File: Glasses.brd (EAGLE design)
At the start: 139.7 x 63.5 mm, 0 parts

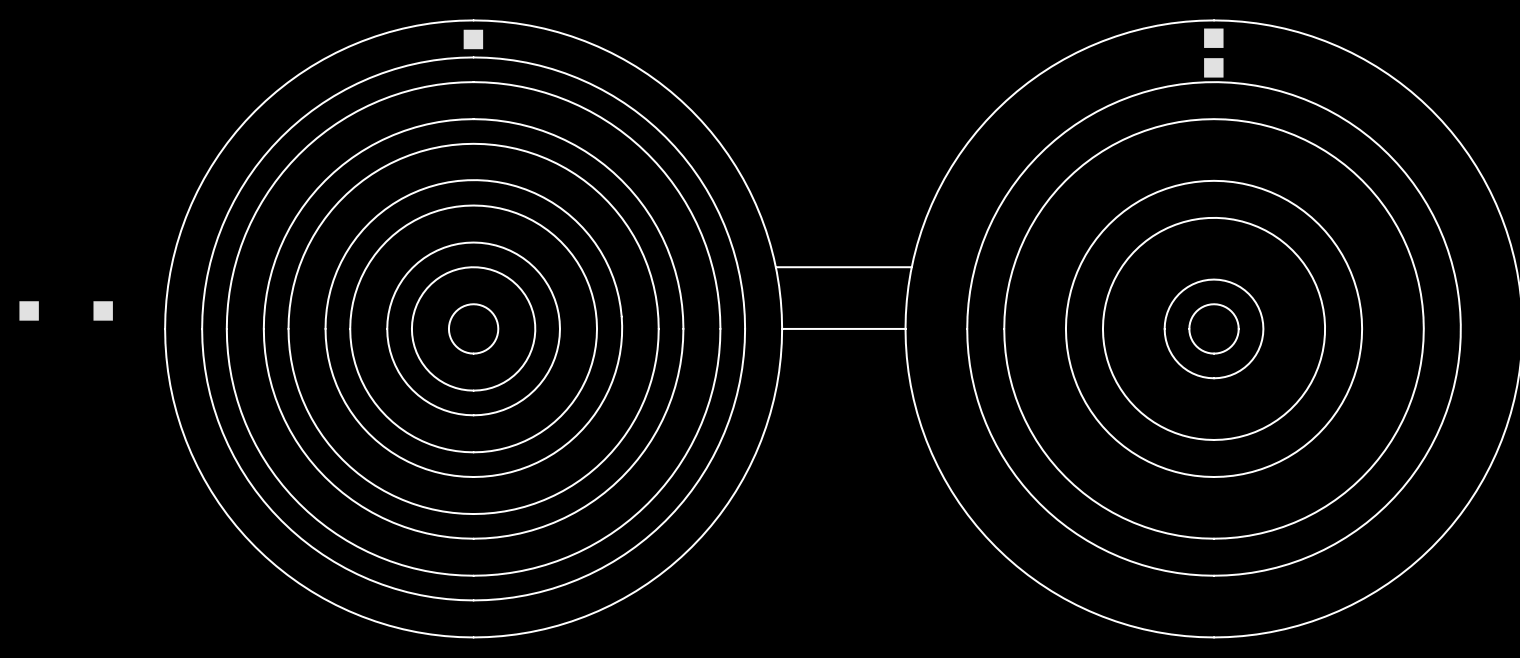
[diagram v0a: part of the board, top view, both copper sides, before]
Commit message: began laying out glasses shape
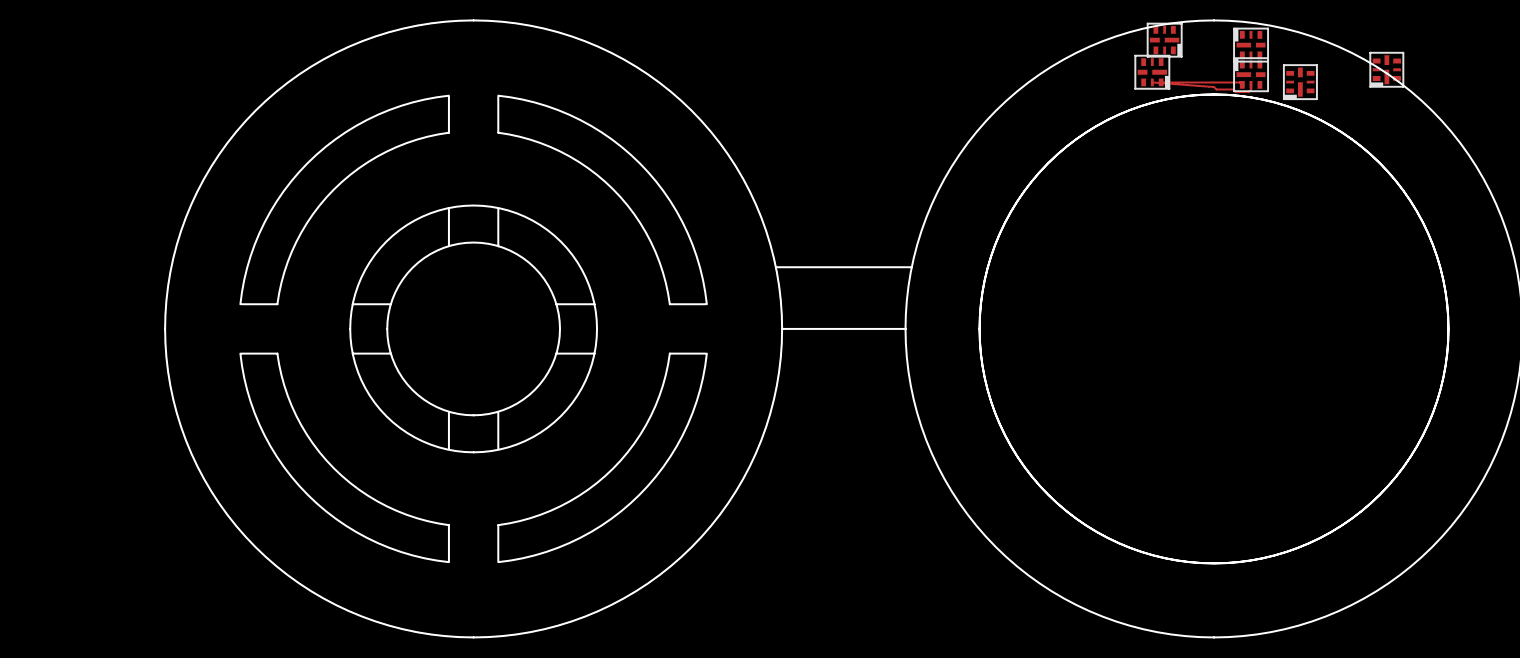
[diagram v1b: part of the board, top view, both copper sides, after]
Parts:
- added FRAME1: FRAME-LETTERNO_PACKAGE, SparkFun-Aesthetics:DUMMY
- added U1, U2, U3, U4, U5, U6: APA1022020, 1_BES_Optoelectronics:APA102-2020
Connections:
- new net GND: U1.GND, U1.GNDPAD, U2.GND, U2.GNDPAD, U3.GND, U3.GNDPAD, U4.GND, U4.GNDPAD, U5.GND, U5.GNDPAD, U6.GND, U6.GNDPAD
- new net N$1: U1.SDO, U2.SDI
- new net N$10: U5.SDO, U6.SDI
- new net N$2: U1.CKO, U2.CKI
- new net N$3: U2.CKO, U3.CKI
- new net N$4: U2.SDO, U3.SDI
- new net N$5: U3.SDO, U4.SDI
- new net N$6: U3.CKO, U4.CKI
- new net N$7: U4.CKO, U5.CKI
- new net N$8: U4.SDO, U5.SDI
- new net N$9: U5.CKO, U6.CKI
- new net VCC: U1.VDD, U1.VDDPAD, U2.VDD, U2.VDDPAD, U3.VDD, U3.VDDPAD, U4.VDD, U4.VDDPAD, U5.VDD, U5.VDDPAD, U6.VDD, U6.VDDPAD
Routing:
- net N$3: track 0.00 -> 11.0 mm
- net N$4: track 0.00 -> 8.47 mm
- added copper zone on layer 1, net N$11
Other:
- outline, holes or cut-outs redrawn

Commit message: Post-print changes
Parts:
- moved U1 32.4 mm to (105.4, 29.2), turned to 45 degrees
- moved U5 27.9 mm to (128.3, 82.5)
- moved U3 27.4 mm to (118.1, 84.6)
- moved U4 26.7 mm to (110.5, 34.3), turned to 45 degrees
- moved U6 25.3 mm to (133.3, 82.5)
- moved U2 24.2 mm to (105.4, 34.3), turned to 135 degrees
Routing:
- net N$3: track 11.0 -> 0.00 mm
- net N$4: track 8.47 -> 0.00 mm
- added copper zone on layer 1, net GND
- removed copper zone on layer 1, net N$11
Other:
- outline, holes or cut-outs redrawn

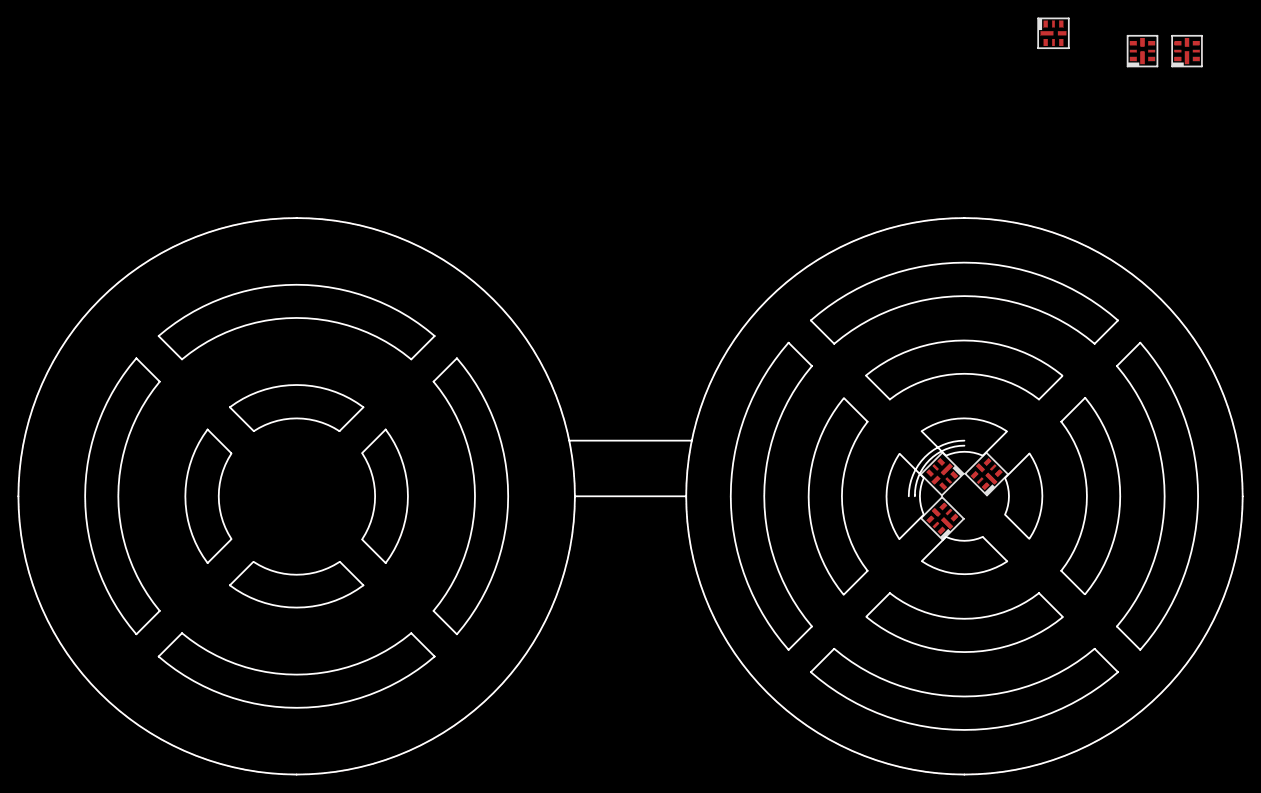
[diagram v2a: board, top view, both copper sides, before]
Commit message: laid out LED's
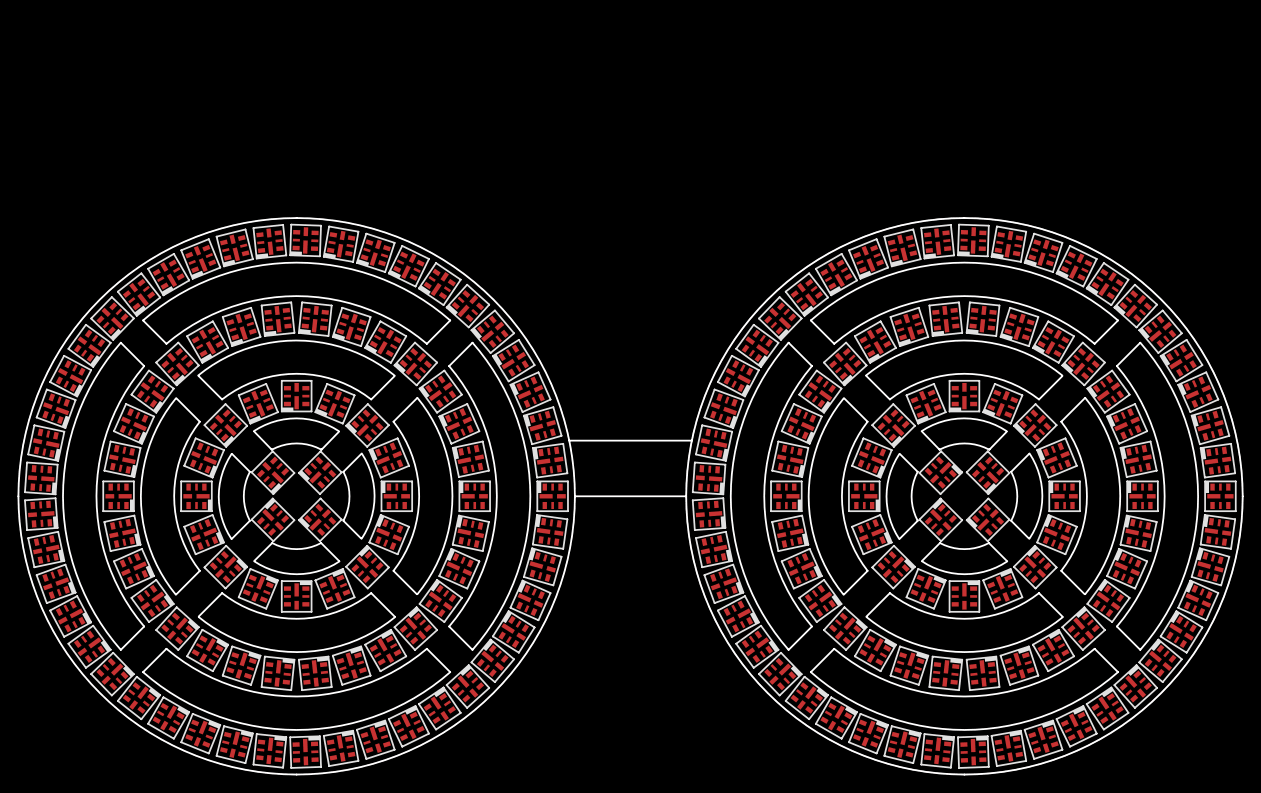
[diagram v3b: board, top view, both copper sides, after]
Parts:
- added FRAME2, FRAME3, FRAME4, FRAME5, FRAME6, FRAME7: FRAME-LETTERNO_PACKAGE, SparkFun-Aesthetics:DUMMY
- added U10, U100, U101, U102, U103, U104, U105, U106, U107, U108, U109, U11, U110, U111, U112, U113, U114, U115, U116, U117, U118, U119, U12, U120, U121, U122, U123, U124, U125, U126, U127, U128, U129, U13, U130, U131, U132, U133, U134, U135, U136, U137, U138, U139, U14, U140, U141, U142, U143, U144, U145, U146, U147, U148, U149, U15, U150, U151, U152, U153, U154, U155, U156, U157, U158, U159, U16, U160, U161, U162, U163, U164, U165, U166, U167, U168, U169, U17, U170, U171, U172, U173, U174, U175, U176, U177, U178, U179, U18, U180, U181, U182, U183, U184, U185, U186, U187, U188, U189, U19, U190, U20, U21, U22, U23, U24, U25, U26, U27, U28, U29, U30, U31, U32, U33, U34, U35, U36, U37, U38, U39, U40, U41, U42, U43, U44, U45, U46, U47, U48, U49, U50, U51, U52, U53, U54, U55, U56, U57, U58, U59, U60, U61, U62, U63, U64, U65, U66, U67, U68, U69, U7, U70, U71, U72, U73, U74, U75, U76, U77, U78, U79, U8, U80, U81, U82, U83, U84, U85, U86, U87, U88, U89, U9, U90, U91, U92, U93, U94, U95, U96, U97, U98, U99: APA1022020, 1_BES_Optoelectronics:APA102-2020
- moved FRAME1 128.7 mm to (71.1, 95.2)
- moved U3 57.0 mm to (105.3, 29.1), turned to 225 degrees
- moved U5 51.6 mm to (119.4, 31.8), turned to 270 degrees
- moved U6 48.7 mm to (118.5, 36.1), turned to 292.5 degrees
- moved U1 7.38 mm to (110.6, 34.4)
- moved U4 5.24 mm to (110.6, 29.1), turned to 315 degrees
- moved U2 0.22 mm to (105.3, 34.4)
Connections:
- new net CK1: U28.CKO, U29.CKI
- new net CK2: U56.CKO, U57.CKI
- new net CK3: U84.CKO, U85.CKI
- new net CK4: U112.CKO, U113.CKI
- new net CK5: U140.CKO, U141.CKI
- new net CK6: U168.CKO, U169.CKI
- new net N$100: U53.SDO, U54.SDI
- new net N$101: U54.CKO, U55.CKI
- new net N$102: U54.SDO, U55.SDI
- new net N$103: U55.CKO, U56.CKI
- new net N$104: U55.SDO, U56.SDI
- new net N$105: U49.SDO, U50.SDI
- new net N$106: U49.CKO, U50.CKI
- new net N$107: U42.SDO, U43.SDI
- new net N$108: U42.CKO, U43.CKI
- new net N$109: U57.SDO, U58.SDI
- new net N$11: U6.CKO, U7.CKI
- new net N$110: U57.CKO, U58.CKI
- new net N$111: U58.CKO, U59.CKI
- new net N$112: U58.SDO, U59.SDI
- new net N$113: U59.SDO, U60.SDI
- new net N$114: U59.CKO, U60.CKI
- new net N$115: U60.CKO, U61.CKI
- new net N$116: U60.SDO, U61.SDI
- new net N$117: U61.CKO, U62.CKI
- new net N$118: U61.SDO, U62.SDI
- new net N$119: U62.CKO, U63.CKI
- new net N$12: U6.SDO, U7.SDI
- new net N$120: U62.SDO, U63.SDI
- new net N$121: U64.SDO, U65.SDI
- new net N$122: U64.CKO, U65.CKI
- new net N$123: U65.CKO, U66.CKI
- new net N$124: U65.SDO, U66.SDI
- new net N$125: U66.SDO, U67.SDI
- new net N$126: U66.CKO, U67.CKI
- new net N$127: U67.CKO, U68.CKI
- new net N$128: U67.SDO, U68.SDI
- new net N$129: U68.CKO, U69.CKI
- new net N$13: U8.SDO, U9.SDI
- new net N$130: U68.SDO, U69.SDI
- new net N$131: U69.CKO, U70.CKI
- new net N$132: U69.SDO, U70.SDI
- new net N$133: U63.SDO, U64.SDI
- new net N$134: U63.CKO, U64.CKI
- new net N$135: U71.SDO, U72.SDI
- new net N$136: U71.CKO, U72.CKI
- new net N$137: U72.CKO, U73.CKI
- new net N$138: U72.SDO, U73.SDI
- new net N$139: U73.SDO, U74.SDI
- new net N$14: U8.CKO, U9.CKI
- new net N$140: U73.CKO, U74.CKI
- new net N$141: U74.CKO, U75.CKI
- new net N$142: U74.SDO, U75.SDI
- new net N$143: U75.CKO, U76.CKI
- new net N$144: U75.SDO, U76.SDI
- new net N$145: U76.CKO, U77.CKI
- new net N$146: U76.SDO, U77.SDI
- new net N$147: U78.SDO, U79.SDI
- new net N$148: U78.CKO, U79.CKI
- new net N$149: U79.CKO, U80.CKI
- new net N$15: U10.CKI, U9.CKO
- new net N$150: U79.SDO, U80.SDI
- new net N$151: U80.SDO, U81.SDI
- new net N$152: U80.CKO, U81.CKI
- new net N$153: U81.CKO, U82.CKI
- new net N$154: U81.SDO, U82.SDI
- new net N$155: U82.CKO, U83.CKI
- new net N$156: U82.SDO, U83.SDI
- new net N$157: U83.CKO, U84.CKI
- new net N$158: U83.SDO, U84.SDI
- new net N$159: U77.SDO, U78.SDI
- new net N$16: U10.SDI, U9.SDO
- new net N$160: U77.CKO, U78.CKI
- new net N$161: U70.SDO, U71.SDI
- new net N$162: U70.CKO, U71.CKI
- new net N$163: U85.SDO, U86.SDI
- new net N$164: U85.CKO, U86.CKI
- new net N$165: U86.CKO, U87.CKI
- new net N$166: U86.SDO, U87.SDI
- new net N$167: U87.SDO, U88.SDI
- new net N$168: U87.CKO, U88.CKI
- new net N$169: U88.CKO, U89.CKI
- new net N$17: U10.SDO, U11.SDI
- new net N$170: U88.SDO, U89.SDI
- new net N$171: U89.CKO, U90.CKI
- new net N$172: U89.SDO, U90.SDI
- new net N$173: U90.CKO, U91.CKI
- new net N$174: U90.SDO, U91.SDI
- new net N$175: U92.SDO, U93.SDI
- new net N$176: U92.CKO, U93.CKI
- new net N$177: U93.CKO, U94.CKI
- new net N$178: U93.SDO, U94.SDI
- new net N$179: U94.SDO, U95.SDI
- new net N$18: U10.CKO, U11.CKI
- new net N$180: U94.CKO, U95.CKI
- new net N$183: U96.CKO, U97.CKI
- new net N$184: U96.SDO, U97.SDI
- new net N$185: U97.CKO, U98.CKI
- new net N$186: U97.SDO, U98.SDI
- new net N$187: U91.SDO, U92.SDI
- new net N$188: U91.CKO, U92.CKI
- new net N$189: U100.SDI, U99.SDO
- new net N$19: U11.CKO, U12.CKI
- new net N$190: U100.CKI, U99.CKO
- new net N$191: U100.CKO, U101.CKI
- new net N$192: U100.SDO, U101.SDI
- new net N$193: U101.SDO, U102.SDI
- new net N$194: U101.CKO, U102.CKI
- new net N$195: U102.CKO, U103.CKI
- new net N$196: U102.SDO, U103.SDI
- new net N$197: U103.CKO, U104.CKI
- new net N$198: U103.SDO, U104.SDI
- new net N$199: U104.CKO, U105.CKI
- new net N$20: U11.SDO, U12.SDI
- new net N$200: U104.SDO, U105.SDI
- new net N$201: U106.SDO, U107.SDI
- new net N$202: U106.CKO, U107.CKI
- new net N$203: U107.CKO, U108.CKI
- new net N$204: U107.SDO, U108.SDI
- new net N$205: U108.SDO, U109.SDI
- new net N$206: U108.CKO, U109.CKI
- new net N$207: U109.CKO, U110.CKI
- new net N$208: U109.SDO, U110.SDI
- new net N$209: U110.CKO, U111.CKI
- new net N$21: U12.CKO, U13.CKI
- new net N$210: U110.SDO, U111.SDI
- new net N$211: U111.CKO, U112.CKI
- new net N$212: U111.SDO, U112.SDI
- new net N$213: U105.SDO, U106.SDI
- new net N$214: U105.CKO, U106.CKI
- new net N$215: U98.SDO, U99.SDI
- new net N$216: U98.CKO, U99.CKI
- new net N$217: U113.SDO, U114.SDI
- new net N$218: U113.CKO, U114.CKI
- new net N$219: U114.CKO, U115.CKI
- new net N$22: U12.SDO, U13.SDI
- new net N$220: U114.SDO, U115.SDI
- new net N$221: U115.SDO, U116.SDI
- new net N$222: U115.CKO, U116.CKI
- new net N$223: U116.CKO, U117.CKI
- new net N$224: U116.SDO, U117.SDI
- new net N$225: U117.CKO, U118.CKI
- new net N$226: U117.SDO, U118.SDI
- new net N$227: U118.CKO, U119.CKI
- new net N$228: U118.SDO, U119.SDI
- new net N$229: U120.SDO, U121.SDI
- new net N$23: U13.CKO, U14.CKI
- new net N$230: U120.CKO, U121.CKI
- new net N$231: U121.CKO, U122.CKI
- new net N$232: U121.SDO, U122.SDI
- new net N$233: U122.SDO, U123.SDI
- new net N$234: U122.CKO, U123.CKI
- new net N$235: U123.CKO, U124.CKI
- new net N$236: U123.SDO, U124.SDI
- new net N$237: U124.CKO, U125.CKI
- new net N$238: U124.SDO, U125.SDI
- new net N$239: U125.CKO, U126.CKI
- new net N$24: U13.SDO, U14.SDI
- new net N$240: U125.SDO, U126.SDI
- new net N$241: U119.SDO, U120.SDI
- new net N$242: U119.CKO, U120.CKI
- new net N$243: U127.SDO, U128.SDI
- new net N$244: U127.CKO, U128.CKI
- new net N$245: U128.CKO, U129.CKI
- new net N$246: U128.SDO, U129.SDI
- new net N$247: U129.SDO, U130.SDI
- new net N$248: U129.CKO, U130.CKI
- new net N$249: U130.CKO, U131.CKI
- new net N$25: U7.SDO, U8.SDI
- new net N$250: U130.SDO, U131.SDI
- new net N$251: U131.CKO, U132.CKI
- new net N$252: U131.SDO, U132.SDI
- new net N$253: U132.CKO, U133.CKI
- new net N$254: U132.SDO, U133.SDI
- new net N$255: U134.SDO, U135.SDI
- new net N$256: U134.CKO, U135.CKI
- new net N$257: U135.CKO, U136.CKI
- new net N$258: U135.SDO, U136.SDI
- new net N$259: U136.SDO, U137.SDI
- new net N$26: U7.CKO, U8.CKI
- new net N$260: U136.CKO, U137.CKI
- new net N$261: U137.CKO, U138.CKI
- new net N$262: U137.SDO, U138.SDI
- new net N$263: U138.CKO, U139.CKI
- new net N$264: U138.SDO, U139.SDI
- new net N$265: U139.CKO, U140.CKI
- new net N$266: U139.SDO, U140.SDI
- new net N$267: U133.SDO, U134.SDI
- new net N$268: U133.CKO, U134.CKI
- new net N$269: U126.SDO, U127.SDI
- new net N$27: U15.SDO, U16.SDI
- new net N$270: U126.CKO, U127.CKI
- new net N$271: U141.SDO, U142.SDI
- new net N$272: U141.CKO, U142.CKI
- new net N$273: U142.CKO, U143.CKI
- new net N$274: U142.SDO, U143.SDI
- new net N$275: U143.SDO, U144.SDI
- new net N$276: U143.CKO, U144.CKI
- new net N$277: U144.CKO, U145.CKI
- new net N$278: U144.SDO, U145.SDI
- new net N$279: U145.CKO, U146.CKI
- new net N$28: U15.CKO, U16.CKI
- new net N$280: U145.SDO, U146.SDI
- new net N$281: U146.CKO, U147.CKI
- new net N$282: U146.SDO, U147.SDI
- new net N$283: U148.SDO, U149.SDI
- new net N$284: U148.CKO, U149.CKI
- new net N$285: U149.CKO, U150.CKI
- new net N$286: U149.SDO, U150.SDI
- new net N$287: U150.SDO, U151.SDI
- new net N$288: U150.CKO, U151.CKI
- new net N$289: U151.CKO, U152.CKI
- new net N$29: U16.CKO, U17.CKI
- new net N$290: U151.SDO, U152.SDI
- new net N$291: U152.CKO, U153.CKI
- new net N$292: U152.SDO, U153.SDI
- new net N$293: U153.CKO, U154.CKI
- new net N$294: U153.SDO, U154.SDI
- new net N$295: U147.SDO, U148.SDI
- new net N$296: U147.CKO, U148.CKI
- new net N$297: U155.SDO, U156.SDI
- new net N$298: U155.CKO, U156.CKI
- new net N$299: U156.CKO, U157.CKI
- new net N$30: U16.SDO, U17.SDI
- new net N$300: U156.SDO, U157.SDI
- new net N$301: U157.SDO, U158.SDI
- new net N$302: U157.CKO, U158.CKI
- new net N$303: U158.CKO, U159.CKI
- new net N$304: U158.SDO, U159.SDI
- new net N$305: U159.CKO, U160.CKI
- new net N$306: U159.SDO, U160.SDI
- new net N$307: U160.CKO, U161.CKI
- new net N$308: U160.SDO, U161.SDI
- new net N$309: U162.SDO, U163.SDI
- new net N$31: U17.SDO, U18.SDI
- new net N$310: U162.CKO, U163.CKI
- new net N$311: U163.CKO, U164.CKI
- new net N$312: U163.SDO, U164.SDI
- new net N$313: U164.SDO, U165.SDI
- new net N$314: U164.CKO, U165.CKI
- new net N$315: U165.CKO, U166.CKI
- new net N$316: U165.SDO, U166.SDI
- new net N$317: U166.CKO, U167.CKI
- new net N$318: U166.SDO, U167.SDI
- new net N$319: U167.CKO, U168.CKI
- new net N$32: U17.CKO, U18.CKI
- new net N$320: U167.SDO, U168.SDI
- new net N$321: U161.SDO, U162.SDI
- new net N$322: U161.CKO, U162.CKI
- new net N$323: U154.SDO, U155.SDI
- new net N$324: U154.CKO, U155.CKI
- new net N$325: U169.SDO, U170.SDI
- new net N$326: U169.CKO, U170.CKI
- new net N$327: U170.CKO, U171.CKI
- new net N$328: U170.SDO, U171.SDI
- new net N$329: U171.SDO, U172.SDI
- new net N$33: U18.CKO, U19.CKI
- new net N$330: U171.CKO, U172.CKI
- new net N$331: U172.CKO, U173.CKI
- new net N$332: U172.SDO, U173.SDI
- new net N$333: U173.CKO, U174.CKI
- new net N$334: U173.SDO, U174.SDI
- new net N$335: U174.CKO, U175.CKI
- new net N$336: U174.SDO, U175.SDI
- new net N$337: U176.SDO, U177.SDI
- new net N$338: U176.CKO, U177.CKI
- new net N$339: U177.CKO, U178.CKI
- new net N$34: U18.SDO, U19.SDI
- new net N$340: U177.SDO, U178.SDI
- new net N$341: U178.SDO, U179.SDI
- new net N$342: U178.CKO, U179.CKI
- new net N$343: U179.CKO, U180.CKI
- new net N$344: U179.SDO, U180.SDI
- new net N$345: U180.CKO, U181.CKI
- new net N$346: U180.SDO, U181.SDI
- new net N$347: U181.CKO, U182.CKI
- new net N$348: U181.SDO, U182.SDI
- new net N$349: U175.SDO, U176.SDI
- new net N$35: U19.CKO, U20.CKI
- new net N$350: U175.CKO, U176.CKI
- new net N$351: U183.SDO, U184.SDI
- new net N$352: U183.CKO, U184.CKI
- new net N$353: U184.CKO, U185.CKI
- new net N$354: U184.SDO, U185.SDI
- new net N$355: U185.SDO, U186.SDI
- new net N$356: U185.CKO, U186.CKI
- new net N$357: U186.CKO, U187.CKI
- new net N$358: U186.SDO, U187.SDI
- new net N$359: U187.CKO, U188.CKI
- new net N$36: U19.SDO, U20.SDI
- new net N$360: U187.SDO, U188.SDI
- new net N$361: U188.CKO, U189.CKI
- new net N$362: U188.SDO, U189.SDI
- new net N$37: U20.CKO, U21.CKI
- new net N$375: U189.SDO, U190.SDI
- new net N$376: U189.CKO, U190.CKI
- new net N$377: U182.SDO, U183.SDI
- new net N$378: U182.CKO, U183.CKI
- new net N$38: U20.SDO, U21.SDI
- new net N$39: U22.SDO, U23.SDI
- new net N$40: U22.CKO, U23.CKI
- new net N$41: U23.CKO, U24.CKI
- new net N$42: U23.SDO, U24.SDI
- new net N$43: U24.SDO, U25.SDI
- new net N$44: U24.CKO, U25.CKI
- new net N$45: U25.CKO, U26.CKI
- new net N$46: U25.SDO, U26.SDI
- new net N$47: U26.CKO, U27.CKI
- new net N$48: U26.SDO, U27.SDI
- new net N$49: U27.CKO, U28.CKI
- new net N$50: U27.SDO, U28.SDI
- new net N$51: U21.SDO, U22.SDI
- new net N$52: U21.CKO, U22.CKI
- new net N$53: U14.SDO, U15.SDI
- new net N$54: U14.CKO, U15.CKI
- new net N$55: U29.SDO, U30.SDI
- new net N$56: U29.CKO, U30.CKI
- new net N$57: U30.CKO, U31.CKI
- new net N$58: U30.SDO, U31.SDI
- new net N$59: U31.SDO, U32.SDI
- new net N$60: U31.CKO, U32.CKI
- new net N$61: U32.CKO, U33.CKI
- new net N$62: U32.SDO, U33.SDI
- new net N$63: U33.CKO, U34.CKI
- new net N$64: U33.SDO, U34.SDI
- new net N$65: U34.CKO, U35.CKI
- new net N$66: U34.SDO, U35.SDI
- new net N$67: U36.SDO, U37.SDI
- new net N$68: U36.CKO, U37.CKI
- new net N$69: U37.CKO, U38.CKI
- new net N$70: U37.SDO, U38.SDI
- new net N$71: U38.SDO, U39.SDI
- new net N$72: U38.CKO, U39.CKI
- new net N$73: U39.CKO, U40.CKI
- new net N$74: U39.SDO, U40.SDI
- new net N$75: U40.CKO, U41.CKI
- new net N$76: U40.SDO, U41.SDI
- new net N$77: U41.CKO, U42.CKI
- new net N$78: U41.SDO, U42.SDI
- new net N$79: U35.SDO, U36.SDI
- new net N$80: U35.CKO, U36.CKI
- new net N$81: U43.SDO, U44.SDI
- new net N$82: U43.CKO, U44.CKI
- new net N$83: U44.CKO, U45.CKI
- new net N$84: U44.SDO, U45.SDI
- new net N$85: U45.SDO, U46.SDI
- new net N$86: U45.CKO, U46.CKI
- new net N$87: U46.CKO, U47.CKI
- new net N$88: U46.SDO, U47.SDI
- new net N$89: U47.CKO, U48.CKI
- new net N$90: U47.SDO, U48.SDI
- new net N$91: U48.CKO, U49.CKI
- new net N$92: U48.SDO, U49.SDI
- new net N$93: U50.SDO, U51.SDI
- new net N$94: U50.CKO, U51.CKI
- new net N$95: U51.CKO, U52.CKI
- new net N$96: U51.SDO, U52.SDI
- new net N$97: U52.SDO, U53.SDI
- new net N$98: U52.CKO, U53.CKI
- new net N$99: U53.CKO, U54.CKI
- new net SD1: U28.SDO, U29.SDI
- new net SD2: U56.SDO, U57.SDI
- new net SD3: U84.SDO, U85.SDI
- new net SD4: U112.SDO, U113.SDI
- new net SD5: U140.SDO, U141.SDI
- new net SD6: U168.SDO, U169.SDI
- net GND: now also U10.GND, U10.GNDPAD, U100.GND, U100.GNDPAD, U101.GND, U101.GNDPAD, U102.GND, U102.GNDPAD, U103.GND, U103.GNDPAD, U104.GND, U104.GNDPAD, U105.GND, U105.GNDPAD, U106.GND, U106.GNDPAD, U107.GND, U107.GNDPAD, U108.GND, U108.GNDPAD, U109.GND, U109.GNDPAD, U11.GND, U11.GNDPAD, U110.GND, U110.GNDPAD, U111.GND, U111.GNDPAD, U112.GND, U112.GNDPAD, U113.GND, U113.GNDPAD, U114.GND, U114.GNDPAD, U115.GND, U115.GNDPAD, U116.GND, U116.GNDPAD, U117.GND, U117.GNDPAD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
- net VCC: now also U10.VDD, U10.VDDPAD, U100.VDD, U100.VDDPAD, U101.VDD, U101.VDDPAD, U102.VDD, U102.VDDPAD, U103.VDD, U103.VDDPAD, U104.VDD, U104.VDDPAD, U105.VDD, U105.VDDPAD, U106.VDD, U106.VDDPAD, U107.VDD, U107.VDDPAD, U108.VDD, U108.VDDPAD, U109.VDD, U109.VDDPAD, U11.VDD, U11.VDDPAD, U110.VDD, U110.VDDPAD, U111.VDD, U111.VDDPAD, U112.VDD, U112.VDDPAD, U113.VDD, U113.VDDPAD, U114.VDD, U114.VDDPAD, U115.VDD, U115.VDDPAD, U116.VDD, U116.VDDPAD, U117.VDD, U117.VDDPAD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
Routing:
- added copper zone on layer 16, net GND
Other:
- outline, holes or cut-outs redrawn

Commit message: changed diameter, began LED layout
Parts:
- removed FRAME1, FRAME2, FRAME3, FRAME4, FRAME5, FRAME6, FRAME7: FRAME-LETTERNO_PACKAGE, SparkFun-Aesthetics:DUMMY
- moved U17 183.9 mm to (276.1, 94.8), turned to 0 degrees
- moved U18 183.3 mm to (278.5, 98.5), turned to 0 degrees
- moved U16 183.1 mm to (272.3, 92.3), turned to 0 degrees
- moved U27 175.1 mm to (274.2, 122.2)
- moved U29 175.1 mm to (265.8, 123.1)
- moved U43 175.1 mm to (265.8, 82.7)
- moved U45 175.1 mm to (274.2, 83.5)
- moved U55 175.1 mm to (292.7, 118.3)
- moved U58 175.1 mm to (284.3, 127.1)
- moved U60 175.1 mm to (277.0, 130.7)
- moved U87 175.1 mm to (277.0, 75.1)
- moved U89 175.1 mm to (284.3, 78.7)
- moved U92 175.1 mm to (292.7, 87.4)
- moved U101 175.1 mm to (202.3, 107.2)
- moved U103 175.1 mm to (196.1, 113.4)
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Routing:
- net VCC: track 0.00 -> 3.39 mm
- added copper zone on layer 1, net VCC
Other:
- board size 139.7 x 63.5 mm -> 299.8 x 134.7 mm

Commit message: laid out footpirnts, routing needed
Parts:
- added J1, J2: (no value), SparkFun-Connectors:1X04_1MM_RA
- added U191, U192, U193, U194, U195, U196, U197, U198, U199, U200, U201, U202, U203, U204, U205, U206, U207, U208, U209, U210, U211, U212, U213, U214, U215, U216, U217, U218, U219, U220, U221, U222, U223, U224, U225, U226, U227, U228, U229, U230, U231, U232, U233, U234, U235, U236, U237, U238, U239, U240, U241, U242, U243, U244, U245, U246, U247, U248, U249, U250, U251, U252: APA1022020, 1_BES_Optoelectronics:APA102-2020
- moved U53 297.7 mm to (11.4, 23.6), turned to 115 degrees
- moved U52 297.7 mm to (9.94, 27.8), turned to 105 degrees
- moved U54 296.6 mm to (13.6, 19.8), turned to 125 degrees
- moved U51 296.6 mm to (9.18, 32.1), turned to 95 degrees
- moved U94 294.7 mm to (14.0, 9.27), turned to 141 degrees
- moved U93 294.6 mm to (10.7, 12.3), turned to 133 degrees
- moved U55 294.5 mm to (16.5, 16.5), turned to 135 degrees
- moved U95 294.0 mm to (17.7, 6.69), turned to 149 degrees
- moved U92 293.7 mm to (7.92, 15.8), turned to 125 degrees
- moved U91 291.9 mm to (5.60, 19.7), turned to 117 degrees
- moved U56 291.3 mm to (19.8, 13.6), turned to 145 degrees
- moved U90 289.4 mm to (3.85, 23.8), turned to 109 degrees
- moved U57 287.1 mm to (23.6, 11.4), turned to 155 degrees
- moved U89 286.1 mm to (2.69, 28.1), turned to 101 degrees
- moved U50 285.5 mm to (9.18, 36.5), turned to 85 degrees
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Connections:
- new net CK7: U196.CKO, U197.CKI
- new net CK8: U224.CKO, U225.CKI
- new net N$365: U190.CKO, U191.CKI
- new net N$366: U190.SDO, U191.SDI
- new net N$367: U191.CKO, U192.CKI
- new net N$368: U191.SDO, U192.SDI
- new net N$369: U192.SDO, U193.SDI
- new net N$370: U192.CKO, U193.CKI
- new net N$371: U193.CKO, U194.CKI
- new net N$372: U193.SDO, U194.SDI
- new net N$373: U194.CKO, U195.CKI
- new net N$374: U194.SDO, U195.SDI
- new net N$379: U195.CKO, U196.CKI
- new net N$380: U195.SDO, U196.SDI
- new net N$381: U197.SDO, U198.SDI
- new net N$382: U197.CKO, U198.CKI
- new net N$383: U198.CKO, U199.CKI
- new net N$384: U198.SDO, U199.SDI
- new net N$385: U199.SDO, U200.SDI
- new net N$386: U199.CKO, U200.CKI
- new net N$387: U200.CKO, U201.CKI
- new net N$388: U200.SDO, U201.SDI
- new net N$389: U201.CKO, U202.CKI
- new net N$390: U201.SDO, U202.SDI
- new net N$391: U202.CKO, U203.CKI
- new net N$392: U202.SDO, U203.SDI
- new net N$393: U204.SDO, U205.SDI
- new net N$394: U204.CKO, U205.CKI
- new net N$395: U205.CKO, U206.CKI
- new net N$396: U205.SDO, U206.SDI
- new net N$397: U206.SDO, U207.SDI
- new net N$398: U206.CKO, U207.CKI
- new net N$399: U207.CKO, U208.CKI
- new net N$400: U207.SDO, U208.SDI
- new net N$401: U208.CKO, U209.CKI
- new net N$402: U208.SDO, U209.SDI
- new net N$403: U209.CKO, U210.CKI
- new net N$404: U209.SDO, U210.SDI
- new net N$405: U203.SDO, U204.SDI
- new net N$406: U203.CKO, U204.CKI
- new net N$407: U211.SDO, U212.SDI
- new net N$408: U211.CKO, U212.CKI
- new net N$409: U212.CKO, U213.CKI
- new net N$410: U212.SDO, U213.SDI
- new net N$411: U213.SDO, U214.SDI
- new net N$412: U213.CKO, U214.CKI
- new net N$413: U214.CKO, U215.CKI
- new net N$414: U214.SDO, U215.SDI
- new net N$415: U215.CKO, U216.CKI
- new net N$416: U215.SDO, U216.SDI
- new net N$417: U216.CKO, U217.CKI
- new net N$418: U216.SDO, U217.SDI
- new net N$419: U217.SDO, U218.SDI
- new net N$420: U217.CKO, U218.CKI
- new net N$421: U210.SDO, U211.SDI
- new net N$422: U210.CKO, U211.CKI
- new net N$423: U219.SDI
- new net N$424: U219.CKI
- new net N$425: U219.CKO, U220.CKI
- new net N$426: U219.SDO, U220.SDI
- new net N$427: U220.SDO, U221.SDI
- new net N$428: U220.CKO, U221.CKI
- new net N$429: U221.CKO, U222.CKI
- new net N$430: U221.SDO, U222.SDI
- new net N$431: U222.CKO, U223.CKI
- new net N$432: U222.SDO, U223.SDI
- new net N$433: U223.CKO, U224.CKI
- new net N$434: U223.SDO, U224.SDI
- new net N$435: U225.SDO, U226.SDI
- new net N$436: U225.CKO, U226.CKI
- new net N$437: U226.CKO, U227.CKI
- new net N$438: U226.SDO, U227.SDI
- new net N$439: U227.SDO, U228.SDI
- new net N$440: U227.CKO, U228.CKI
- new net N$441: U228.CKO, U229.CKI
- new net N$442: U228.SDO, U229.SDI
- new net N$443: U229.CKO, U230.CKI
- new net N$444: U229.SDO, U230.SDI
- new net N$445: U230.CKO, U231.CKI
- new net N$446: U230.SDO, U231.SDI
- new net N$447: U232.SDO, U233.SDI
- new net N$448: U232.CKO, U233.CKI
- new net N$449: U233.CKO, U234.CKI
- new net N$450: U233.SDO, U234.SDI
- new net N$451: U234.SDO, U235.SDI
- new net N$452: U234.CKO, U235.CKI
- new net N$453: U235.CKO, U236.CKI
- new net N$454: U235.SDO, U236.SDI
- new net N$455: U236.CKO, U237.CKI
- new net N$456: U236.SDO, U237.SDI
- new net N$457: U237.CKO, U238.CKI
- new net N$458: U237.SDO, U238.SDI
- new net N$459: U231.SDO, U232.SDI
- new net N$460: U231.CKO, U232.CKI
- new net N$461: U239.SDO, U240.SDI
- new net N$462: U239.CKO, U240.CKI
- new net N$463: U240.CKO, U241.CKI
- new net N$464: U240.SDO, U241.SDI
- new net N$465: U241.SDO, U242.SDI
- new net N$466: U241.CKO, U242.CKI
- new net N$467: U242.CKO, U243.CKI
- new net N$468: U242.SDO, U243.SDI
- new net N$469: U243.CKO, U244.CKI
- new net N$470: U243.SDO, U244.SDI
- new net N$471: U244.CKO, U245.CKI
- new net N$472: U244.SDO, U245.SDI
- new net N$473: U245.SDO, U246.SDI
- new net N$474: U245.CKO, U246.CKI
- new net N$475: U238.SDO, U239.SDI
- new net N$476: U238.CKO, U239.CKI
- new net N$477: U247.SDI
- new net N$478: U247.CKI
- new net N$479: U247.CKO, U248.CKI
- new net N$480: U247.SDO, U248.SDI
- new net N$481: U248.SDO, U249.SDI
- new net N$482: U248.CKO, U249.CKI
- new net N$483: U249.CKO, U250.CKI
- new net N$484: U249.SDO, U250.SDI
- new net N$485: U250.CKO, U251.CKI
- new net N$486: U250.SDO, U251.SDI
- new net N$487: U251.CKO, U252.CKI
- new net N$488: U251.SDO, U252.SDI
- new net N$489: U127.CKI
- new net N$490: J1.3, U126.SDO
- new net N$491: J2.4, U252.CKO
- new net N$492: J2.3, U252.SDO
- new net SD7: U196.SDO, U197.SDI
- new net SD8: U224.SDO, U225.SDI
- net GND: now also J1.1, J2.1, U191.GND, U191.GNDPAD, U192.GND, U192.GNDPAD, U193.GND, U193.GNDPAD, U194.GND, U194.GNDPAD, U195.GND, U195.GNDPAD, U196.GND, U196.GNDPAD, U197.GND, U197.GNDPAD, U198.GND, U198.GNDPAD, U199.GND, U199.GNDPAD, U200.GND, U200.GNDPAD, U201.GND, U201.GNDPAD, U202.GND, U202.GNDPAD, U203.GND, U203.GNDPAD, U204.GND, U204.GNDPAD, U205.GND, U205.GNDPAD, U206.GND, U206.GNDPAD, U207.GND, U207.GNDPAD, U208.GND, U208.GNDPAD, U209.GND, U209.GNDPAD, U210.GND, U210.GNDPAD, U211.GND, U211.GNDPAD, U212.GND, U212.GNDPAD, U213.GND, U213.GNDPAD, U214.GND, U214.GNDPAD, U215.GND, U215.GNDPAD, U216.GND, U216.GNDPAD, U217.GND, U217.GNDPAD, U218.GND, U218.GNDPAD, U219.GND, U219.GNDPAD, U220.GND, U220.GNDPAD, U221.GND, U221.GNDPAD, U222.GND, U222.GNDPAD, U223.GND, U223.GNDPAD, U224.GND, U224.GNDPAD, U225.GND, U225.GNDPAD, U226.GND, U226.GNDPAD, U227.GND, U227.GNDPAD, U228.GND, U228.GNDPAD, U229.GND, U229.GNDPAD, U230.GND, U230.GNDPAD, U231.GND, U231.GNDPAD, U232.GND, U232.GNDPAD, U233.GND, U233.GNDPAD, U234.GND, U234.GNDPAD, U235.GND, U235.GNDPAD, U236.GND, U236.GNDPAD, U237.GND, U237.GNDPAD, U238.GND, U238.GNDPAD, U239.GND, U239.GNDPAD, U240.GND, U240.GNDPAD, U241.GND, U241.GNDPAD, U242.GND, U242.GNDPAD, U243.GND, U243.GNDPAD, U244.GND, U244.GNDPAD, U245.GND, U245.GNDPAD, U246.GND, U246.GNDPAD, U247.GND, U247.GNDPAD, U248.GND, U248.GNDPAD, U249.GND, U249.GNDPAD, U250.GND, U250.GNDPAD, U251.GND, U251.GNDPAD, U252.GND, U252.GNDPAD
- net N$269: no longer U126.SDO
- net N$270: now also J1.4; no longer U127.CKI
- net VCC: now also J1.2, J2.2, U191.VDD, U191.VDDPAD, U192.VDD, U192.VDDPAD, U193.VDD, U193.VDDPAD, U194.VDD, U194.VDDPAD, U195.VDD, U195.VDDPAD, U196.VDD, U196.VDDPAD, U197.VDD, U197.VDDPAD, U198.VDD, U198.VDDPAD, U199.VDD, U199.VDDPAD, U200.VDD, U200.VDDPAD, U201.VDD, U201.VDDPAD, U202.VDD, U202.VDDPAD, U203.VDD, U203.VDDPAD, U204.VDD, U204.VDDPAD, U205.VDD, U205.VDDPAD, U206.VDD, U206.VDDPAD, U207.VDD, U207.VDDPAD, U208.VDD, U208.VDDPAD, U209.VDD, U209.VDDPAD, U210.VDD, U210.VDDPAD, U211.VDD, U211.VDDPAD, U212.VDD, U212.VDDPAD, U213.VDD, U213.VDDPAD, U214.VDD, U214.VDDPAD, U215.VDD, U215.VDDPAD, U216.VDD, U216.VDDPAD, U217.VDD, U217.VDDPAD, U218.VDD, U218.VDDPAD, U219.VDD, U219.VDDPAD, U220.VDD, U220.VDDPAD, U221.VDD, U221.VDDPAD, U222.VDD, U222.VDDPAD, U223.VDD, U223.VDDPAD, U224.VDD, U224.VDDPAD, U225.VDD, U225.VDDPAD, U226.VDD, U226.VDDPAD, U227.VDD, U227.VDDPAD, U228.VDD, U228.VDDPAD, U229.VDD, U229.VDDPAD, U230.VDD, U230.VDDPAD, U231.VDD, U231.VDDPAD, U232.VDD, U232.VDDPAD, U233.VDD, U233.VDDPAD, U234.VDD, U234.VDDPAD, U235.VDD, U235.VDDPAD, U236.VDD, U236.VDDPAD, U237.VDD, U237.VDDPAD, U238.VDD, U238.VDDPAD, U239.VDD, U239.VDDPAD, U240.VDD, U240.VDDPAD, U241.VDD, U241.VDDPAD, U242.VDD, U242.VDDPAD, U243.VDD, U243.VDDPAD, U244.VDD, U244.VDDPAD, U245.VDD, U245.VDDPAD, U246.VDD, U246.VDDPAD, U247.VDD, U247.VDDPAD, U248.VDD, U248.VDDPAD, U249.VDD, U249.VDDPAD, U250.VDD, U250.VDDPAD, U251.VDD, U251.VDDPAD, U252.VDD, U252.VDDPAD
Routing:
- net VCC: track 3.39 -> 0.00 mm
- removed copper zone on layer 16, net GND
- removed copper zone on layer 1, net VCC
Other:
- board size 299.8 x 134.7 mm -> 147.4 x 68.7 mm
